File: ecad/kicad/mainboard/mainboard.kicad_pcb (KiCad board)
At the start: 2 copper layers, 99.1 x 81.3 mm, 34 parts, among them IC1 74HC86, J1 SENSORS, J2 CONN_06SILK_FEMALE_PTH, J3 CONN_06SILK_FEMALE_PTH, J4 POWER, J5 SERIAL, M1 Left Motor, M2 Right Motor, U1 Arduino_Nano, U2 TB6612FNG-Module

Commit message: Zwischenstand: IBOM, Layout
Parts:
- added FID1: Fiducial_0.75mm_Mask1.5mm, Fiducial:Fiducial_0.75mm_Mask1.5mm, F.Cu at (70.0, 141.0)
- added FID2: Fiducial_0.75mm_Mask1.5mm, Fiducial:Fiducial_0.75mm_Mask1.5mm, F.Cu at (73.0, 71.5)
- added FID3: Fiducial_0.75mm_Mask1.5mm, Fiducial:Fiducial_0.75mm_Mask1.5mm, F.Cu at (152.0, 72.0)
- moved D3 2.51 mm to (117.0, 90.5)
- moved D1 0.43 mm to (116.8, 113.0)
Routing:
- net GND: track 0.00 -> 63.6 mm, vias 0 -> 4
- net /FUNCTION_SELECT: track 135.7 -> 122.8 mm
- net /RXD: track 8.88 -> 6.18 mm
- net //RIGHT_DIR: track 44.0 -> 41.4 mm, vias 1 -> 3
- net /LEFT_A: track 52.2 -> 50.2 mm
- net //LEFT_DIR: track 24.3 -> 22.8 mm, vias 0 -> 2
- net /LEFT_MOTOR_2: track 46.7 -> 48.1 mm
- net Net-(R5-Pad2): track 60.2 -> 59.0 mm
- net /RIGHT_B: track 47.6 -> 46.5 mm
- net /LEFT_MOTOR_1: track 48.2 -> 49.0 mm
- net /RIGHT_A: track 48.3 -> 47.5 mm
- net /LEFT_B: track 48.6 -> 47.9 mm
- net /RIGHT_DIR: track 88.0 -> 88.7 mm
- net 5V: track 238.5 -> 238.0 mm, vias 4 -> 0
- net /SW_PWR: track 74.6 -> 74.9 mm, vias 0 -> 1

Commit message: Zwischenstand Layout
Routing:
- net GND: track 63.6 -> 118.2 mm, vias 4 -> 3
- net 5V: track 238.0 -> 221.3 mm
- net /RIGHT_DIR: track 88.7 -> 73.3 mm, vias 3 -> 2
- net /RIGHT_PWM: track 48.2 -> 44.4 mm, vias 2 -> 1
- net //RIGHT_DIR: track 41.4 -> 43.4 mm
- net /LEFT_MOTOR_1: track 49.0 -> 49.9 mm
- net /RIGHT_MOTOR_1: track 32.3 -> 33.1 mm, vias 1 -> 0
- net /3V3: track 14.3 -> 15.0 mm
- net /LEFT_MOTOR_2: track 48.1 -> 48.6 mm
- net /LEFT_DIR: track 46.7 -> 46.2 mm, vias 2 -> 1
- net /V_BATT: track 86.5 -> 86.7 mm, vias 2 -> 1
- net /RIGHT_MOTOR_2: track 32.1 -> 32.3 mm, vias 1 -> 0

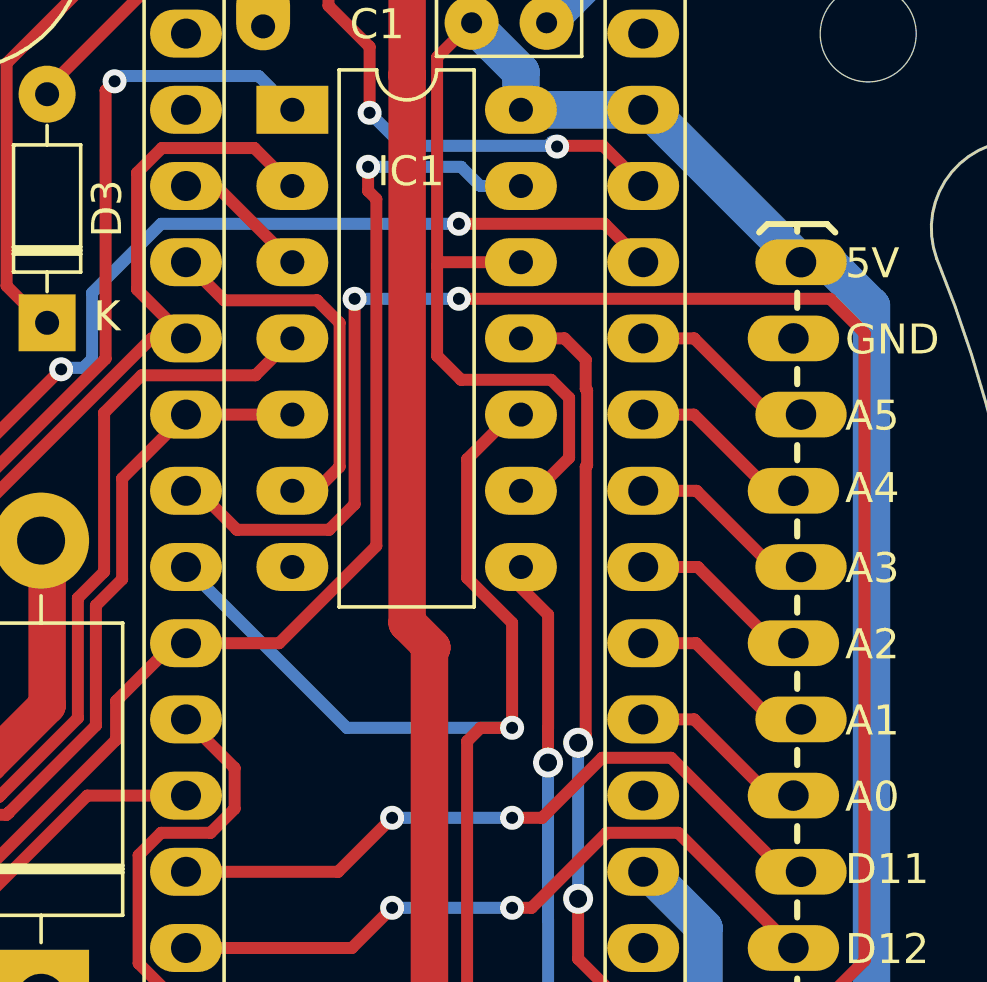
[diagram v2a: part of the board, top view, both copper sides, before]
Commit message: changed pads to connected layer only
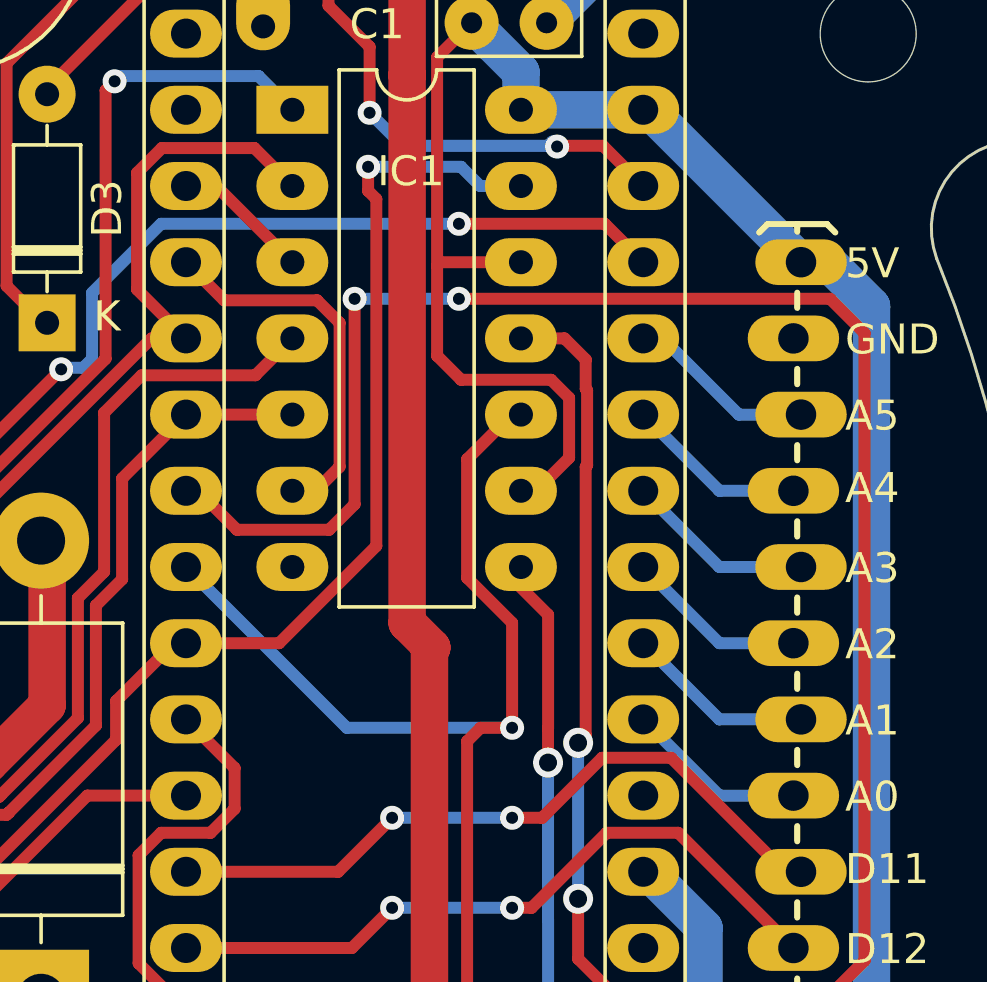
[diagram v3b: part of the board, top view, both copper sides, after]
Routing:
- net /SENSOR_5: track 5.29 -> 7.33 mm
- net /SENSOR_0: track 4.89 -> 6.83 mm
- net /SENSOR_1: track 5.35 -> 7.27 mm
- net /SENSOR_3: track 5.37 -> 7.25 mm
- net /SENSOR_4: track 5.28 -> 6.84 mm
- net /LEFT_CLK_A: track 3.59 -> 4.60 mm
- net /SENSOR_2: track 5.41 -> 6.06 mm

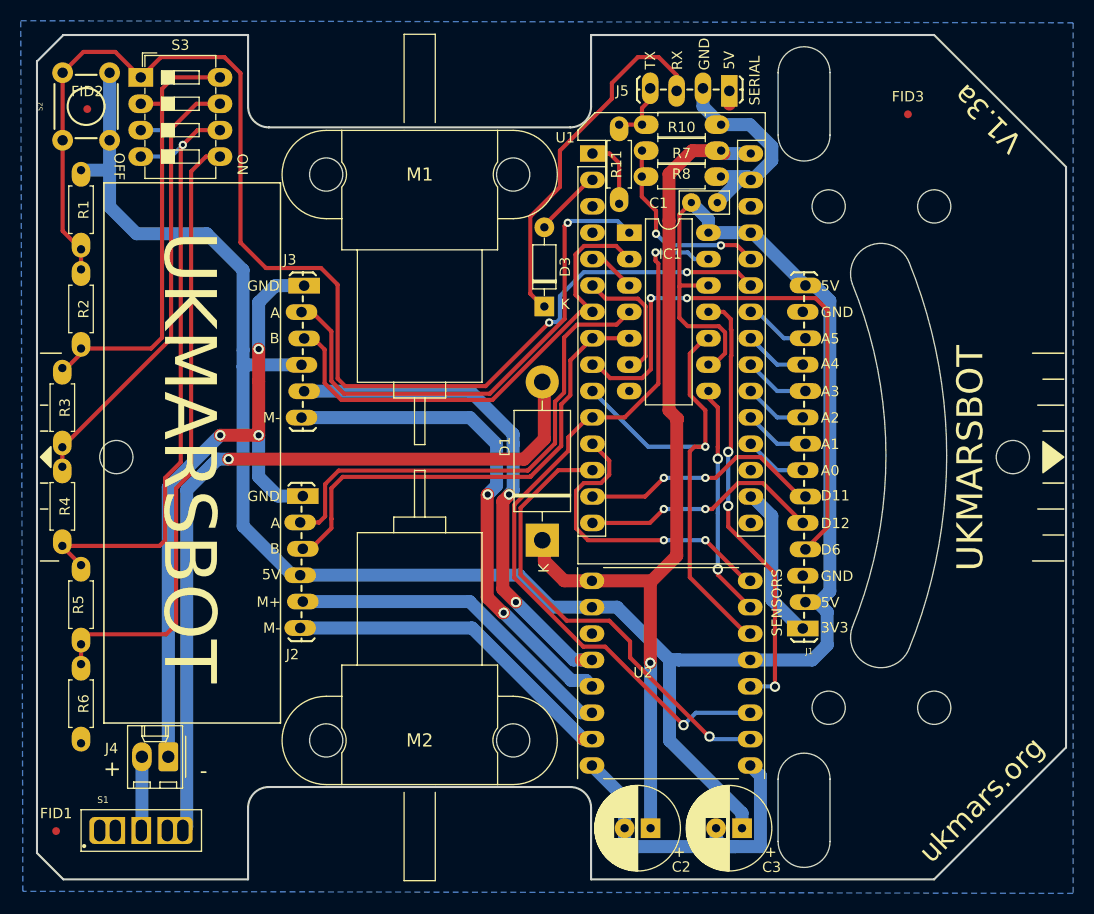
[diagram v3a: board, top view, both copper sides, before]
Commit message: changed all pads to connected layer only
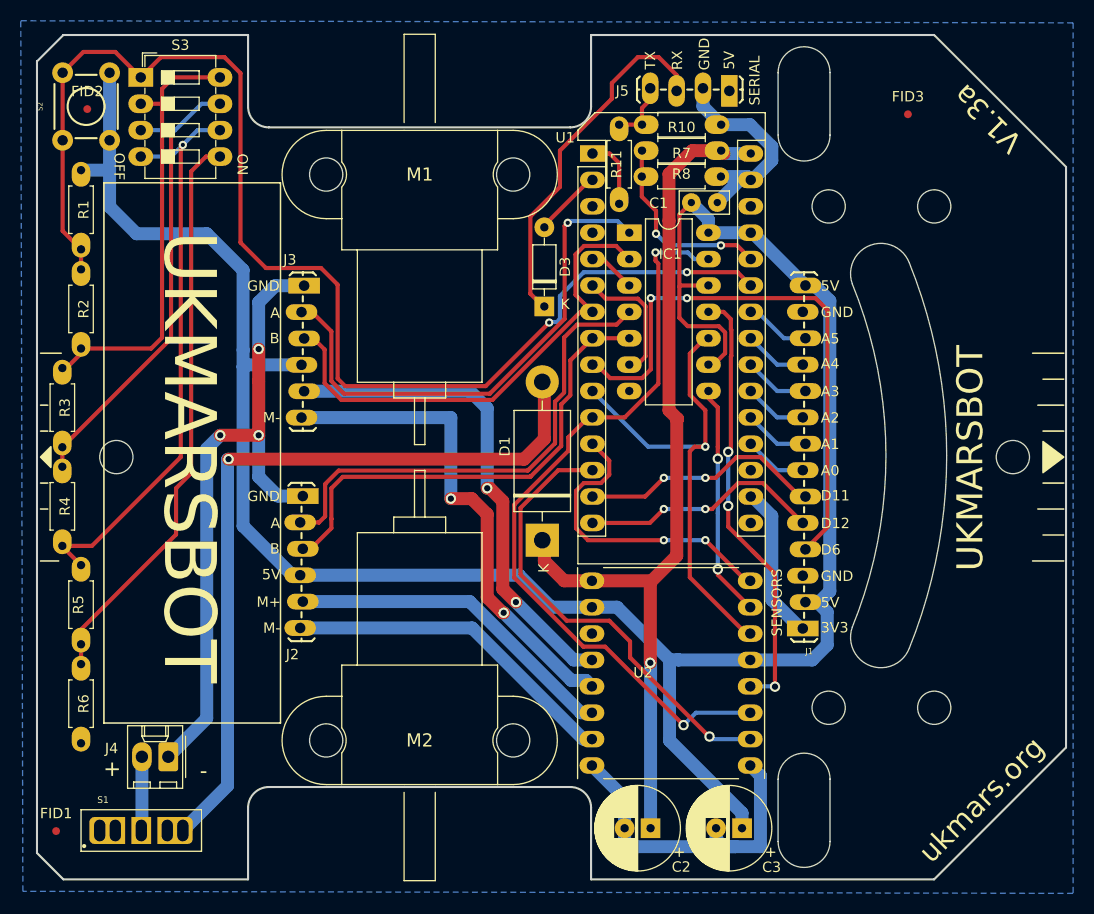
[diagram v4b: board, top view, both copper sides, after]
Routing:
- net Net-(R5-Pad2): track 59.0 -> 54.2 mm
- net Net-(R4-Pad1): track 59.7 -> 56.3 mm
- net /LEFT_MOTOR_1: track 49.9 -> 47.9 mm
- net 5V: track 221.3 -> 220.0 mm
- net /TXD_BT: track 4.92 -> 6.03 mm
- net /SENSOR_5: track 7.33 -> 6.31 mm
- net /SENSOR_1: track 7.27 -> 6.31 mm
- net /SENSOR_3: track 7.25 -> 6.31 mm
- net /SENSOR_4: track 6.84 -> 6.06 mm
- net /RIGHT_CLK_A: track 11.9 -> 12.7 mm
- net /SENSOR_0: track 6.83 -> 6.06 mm
- net /LEFT_MOTOR_2: track 48.6 -> 47.9 mm
- net /RIGHT_MOTOR_1: track 33.1 -> 32.5 mm
- net /SW_PWR: track 74.9 -> 74.3 mm
